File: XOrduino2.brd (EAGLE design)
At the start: 81.3 x 59.8 mm, 82 parts, among them J1 2.5mm, J2 2.5mm, J3 2.5mm, J4 2.5mm, J5 Batt In, J6 MOT R, J7 MOT L, P1 10k, Q1 ALS-PT204-6C/L177, SW1 RESET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

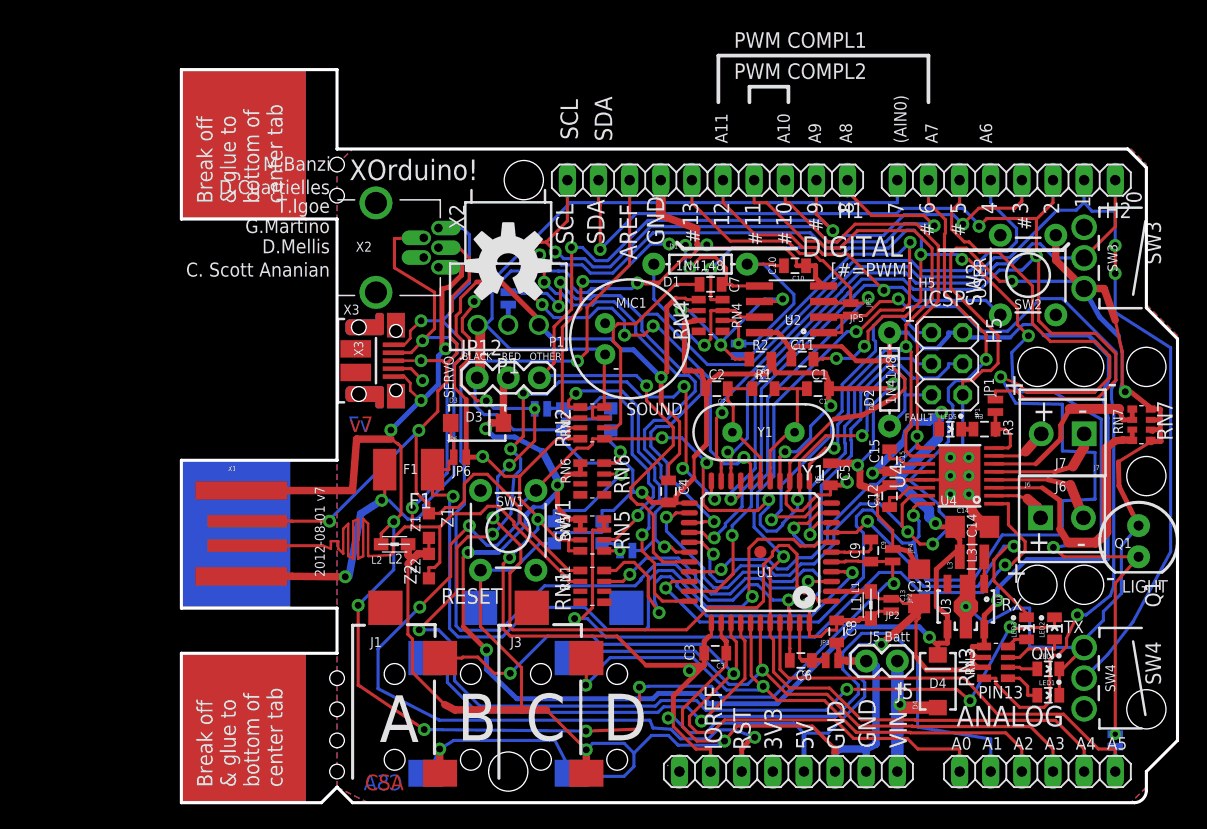
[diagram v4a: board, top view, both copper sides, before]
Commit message: Minor silkscreen tweaks, extend L3 pads a hair.
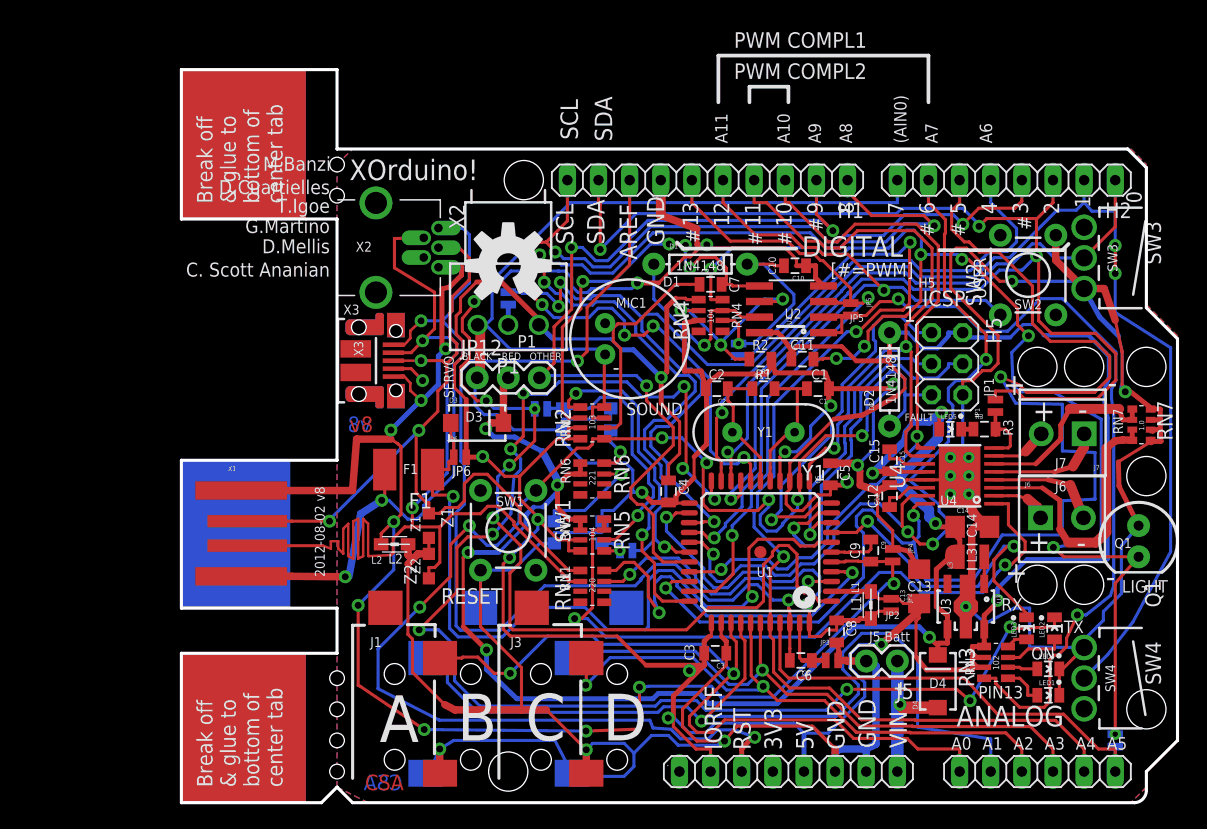
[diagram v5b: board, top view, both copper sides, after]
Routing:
- net VCCIO: track 125.0 -> 126.1 mm
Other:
- board text added: "1.0"
- board text added: "102"
- board text added: "103"
- board text added: "104"
- board text added: "2012-08-02 v8"
- board text added: "220"
- board text added: "221"
- board text added: "v8"
- board text removed: "2012-08-01 v7"
- board text removed: "v7"
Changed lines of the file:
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@@
 <setting verticaltext="up"/>
 </settings>
-<grid distance="5" unitdist="mil" unit="mil" style="lines" multiple="1" display="yes" altdistance="8" altunitdist="mil" altunit="mil"/>
+<grid distance="5" unitdist="mil" unit="mil" style="lines" multiple="1" display="yes" altdistance="1" altunitdist="mil" altunit="mil"/>
 <layers>
 <layer number="1" name="Top" color="4" fill="1" visible="yes" active="yes"/>
-<layer number="2" name="Route2" color="1" fill="3" visible="yes" active="yes"/>
+<layer number="2" name="Route2" color="1" fill="3" visible="no" active="yes"/>
 <layer number="3" name="Route3" color="4" fill="3" visible="no" active="no"/>
 <layer number="4" name="Route4" color="1" fill="4" visible="no" active="no"/>
@@
 <layer number="13" name="Route13" color="4" fill="5" visible="no" active="no"/>
 <layer number="14" name="Route14" color="1" fill="6" visible="no" active="no"/>
-<layer number="15" name="Route15" color="4" fill="6" visible="yes" active="yes"/>
-<layer number="16" name="Bottom" color="1" fill="1" visible="yes" active="yes"/>
+<layer number="15" name="Route15" color="4" fill="6" visible="no" active="yes"/>
+<layer number="16" name="Bottom" color="1" fill="1" visible="no" active="yes"/>
 <layer number="17" name="Pads" color="2" fill="1" visible="yes" active="yes"/>
 <layer number="18" name="Vias" color="14" fill="1" visible="yes" active="yes"/>
@@
 <layer number="20" name="Dimension" color="15" fill="2" visible="yes" active="yes"/>
 <layer number="21" name="tPlace" color="7" fill="1" visible="yes" active="yes"/>
-<layer number="22" name="bPlace" color="7" fill="1" visible="yes" active="yes"/>
-<layer number="23" name="tOrigins" color="15" fill="1" visible="yes" active="yes"/>
+<layer number="22" name="bPlace" color="7" fill="1" visible="no" active="yes"/>
+<layer number="23" name="tOrigins" color="15" fill="1" visible="no" active="yes"/>
 <layer number="24" name="bOrigins" color="15" fill="1" visible="no" active="yes"/>
 <layer number="25" name="tNames" color="5" fill="1" visible="no" active="yes"/>
@@
 <layer number="27" name="tValues" color="7" fill="1" visible="no" active="yes"/>
 <layer number="28" name="bValues" color="7" fill="1" visible="no" active="yes"/>
-<layer number="29" name="tStop" color="2" fill="3" visible="yes" active="yes"/>
-<layer number="30" name="bStop" color="5" fill="6" visible="yes" active="yes"/>
-<layer number="31" name="tCream" color="7" fill="4" visible="yes" active="yes"/>
-<layer number="32" name="bCream" color="7" fill="5" visible="yes" active="yes"/>
+<layer number="29" name="tStop" color="2" fill="3" visible="no" active="yes"/>
+<layer number="30" name="bStop" color="5" fill="6" visible="no" active="yes"/>
+<layer number="31" name="tCream" color="7" fill="4" visible="no" active="yes"/>
+<layer number="32" name="bCream" color="7" fill="5" visible="no" active="yes"/>
 <layer number="33" name="tFinish" color="6" fill="3" visible="no" active="yes"/>
 <layer number="34" name="bFinish" color="6" fill="6" visible="no" active="yes"/>
@@
 <layer number="37" name="tTest" color="7" fill="1" visible="no" active="yes"/>
 <layer number="38" name="bTest" color="7" fill="1" visible="no" active="yes"/>
-<layer number="39" name="tKeepout" color="4" fill="11" visible="yes" active="yes"/>
-<layer number="40" name="bKeepout" color="1" fill="11" visible="yes" active="yes"/>
-<layer number="41" name="tRestrict" color="4" fill="10" visible="yes" active="yes"/>
-<layer number="42" name="bRestrict" color="1" fill="10" visible="yes" active="yes"/>
-<layer number="43" name="vRestrict" color="2" fill="10" visible="yes" active="yes"/>
+<layer number="39" name="tKeepout" color="4" fill="11" visible="no" active="yes"/>
+<layer number="40" name="bKeepout" color="1" fill="11" visible="no" active="yes"/>
+<layer number="41" name="tRestrict" color="4" fill="10" visible="no" active="yes"/>
+<layer number="42" name="bRestrict" color="1" fill="10" visible="no" active="yes"/>
+<layer number="43" name="vRestrict" color="2" fill="10" visible="no" active="yes"/>
 <layer number="44" name="Drills" color="7" fill="1" visible="yes" active="yes"/>
 <layer number="45" name="Holes" color="7" fill="1" visible="yes" active="yes"/>
@@
 <text x="12.1158" y="47.625" size="1.143" layer="25" font="vector" ratio="12" rot="R180">G.Martino</text>
 <text x="12.1158" y="49.276" size="1.143" layer="25" font="vector" ratio="12" rot="R180">T.Igoe</text>
-<text x="11.6982" y="22.1198" size="0.8128" layer="21" font="vector" ratio="12" rot="R90" align="bottom-center">2012-08-01 v7</text>
+<text x="11.6982" y="22.1198" size="0.8128" layer="21" font="vector" ratio="12" rot="R90" align="bottom-center">2012-08-02 v8</text>
 <text x="46.4522" y="4.3048" size="1.4224" layer="21" font="vector" ratio="10" rot="R90">RST</text>
 <text x="48.9922" y="4.3048" size="1.4224" layer="21" font="vector" ratio="10" rot="R90">3V3</text>
@@
 <text x="12.1158" y="44.069" size="1.143" layer="25" font="vector" ratio="12" rot="R180">C. Scott Ananian</text>
 <text x="14.986" y="1.016" size="1.27" layer="1" ratio="20">CSA</text>
-<text x="14.525" y="30.878" size="1.27" layer="16" ratio="20" rot="MR180" align="center">v7</text>
+<text x="14.525" y="30.878" size="1.27" layer="16" ratio="20" rot="MR180" align="center">v8</text>
 <text x="13.716" y="50.8" size="1.6764" layer="21" ratio="15">XOrduino!</text>
 <hole x="78.74" y="26.65" drill="3.2"/>
@@
 <text x="55.372" y="8.763" size="1.27" layer="21" ratio="25">-</text>
 <text x="21.1836" y="16.2306" size="1.27" layer="21" ratio="22">RESET</text>
-<text x="14.685" y="30.878" size="1.27" layer="1" ratio="20" rot="R180" align="center">v7</text>
+<text x="14.685" y="30.878" size="1.27" layer="1" ratio="20" rot="R180" align="center">v8</text>
 <text x="13.462" y="54.864" size="1.778" layer="51" ratio="15">XOrduino!</text>
 <text x="18.034" y="1.016" size="1.27" layer="16" ratio="20" rot="MR0">CSA</text>
@@
 <text x="47.244" y="36.957" size="0.8128" layer="21" ratio="22" align="bottom-center">R2</text>
 <text x="50.673" y="36.957" size="0.8128" layer="21" ratio="22" align="bottom-center">C11</text>
-<text x="49.911" y="38.989" size="0.8128" layer="21" ratio="22" align="bottom-center">U2</text>
+<text x="49.911" y="39.497" size="0.8128" layer="21" ratio="22" align="bottom-center">U2</text>
 <text x="45.72" y="39.751" size="0.8128" layer="21" ratio="22" rot="R90" align="bottom-center">RN4</text>
 <text x="48.514" y="43.815" size="0.6096" layer="21" ratio="22" rot="R90" align="bottom-center">C10</text>
@@
 <text x="44.704" y="42.291" size="0.8128" layer="21" ratio="22" rot="R270" align="bottom-center">C7</text>
 <text x="36.703" y="40.386" size="0.8128" layer="21" ratio="22" align="bottom-center">MIC1</text>
-<text x="30.607" y="37.211" size="0.8128" layer="21" ratio="22" align="bottom-center">P1</text>
+<text x="28.194" y="37.1348" size="1.016" layer="21" ratio="22" align="bottom-center">P1</text>
 <text x="24.13" y="36.1188" size="0.6096" layer="21" ratio="22" align="bottom-center">BLACK</text>
 <text x="26.924" y="36.1188" size="0.6096" layer="21" ratio="22" align="bottom-center">RED</text>
@@
 <text x="27.813" y="42.037" size="0.8128" layer="22" ratio="22" rot="MR0">JP9</text>
 <text x="50.165" y="45.72" size="1.016" layer="22" ratio="22" rot="MR0">Cut JP6 if populating U3</text>
+<wire x1="48.641" y1="38.862" x2="50.8" y2="38.862" width="0.254" layer="21"/>
+<text x="43.434" y="39.116" size="0.508" layer="21" ratio="20" rot="R90">104</text>
+<text x="33.782" y="21.3106" size="0.508" layer="21" ratio="20" rot="R90">104</text>
+<text x="33.782" y="30.4546" size="0.508" layer="21" ratio="20" rot="R90">103</text>
+<text x="33.782" y="25.908" size="0.508" layer="21" ratio="20" rot="R90">221</text>
+<text x="33.782" y="17.145" size="0.508" layer="21" ratio="20" rot="R90">220</text>
+<text x="66.7258" y="10.8204" size="0.508" layer="21" ratio="20" rot="R90">102</text>
+<text x="78.5622" y="30.353" size="0.4318" layer="21" ratio="20" rot="R90">1.0</text>
+<rectangle x1="62.23" y1="18.9738" x2="63.119" y2="21.1836" layer="29"/>
 </plain>
 <attributes>
@@
 <wire x1="32.553" y1="27.711" x2="32.553" y2="26.816" width="0.4064" layer="1"/>
 <wire x1="61.722" y1="30.988" x2="62.0232" y2="31.864" width="0.8128" layer="16"/>
+<wire x1="63.0428" y1="20.3454" x2="63.0428" y2="20.066" width="1.4224" layer="1"/>
+<wire x1="63.0428" y1="20.066" x2="63.0428" y2="19.7866" width="1.4224" layer="1"/>
+<wire x1="63.516" y1="20.066" x2="63.0428" y2="20.066" width="0.4064" layer="1"/>
 </signal>
 <signal name="PAD">
